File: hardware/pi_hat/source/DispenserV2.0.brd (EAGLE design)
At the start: 65 x 56 mm, 11 parts, among them J10 455-1750-1-ND, J11 455-1750-1-ND, J9 455-1750-1-ND, U2 A4988

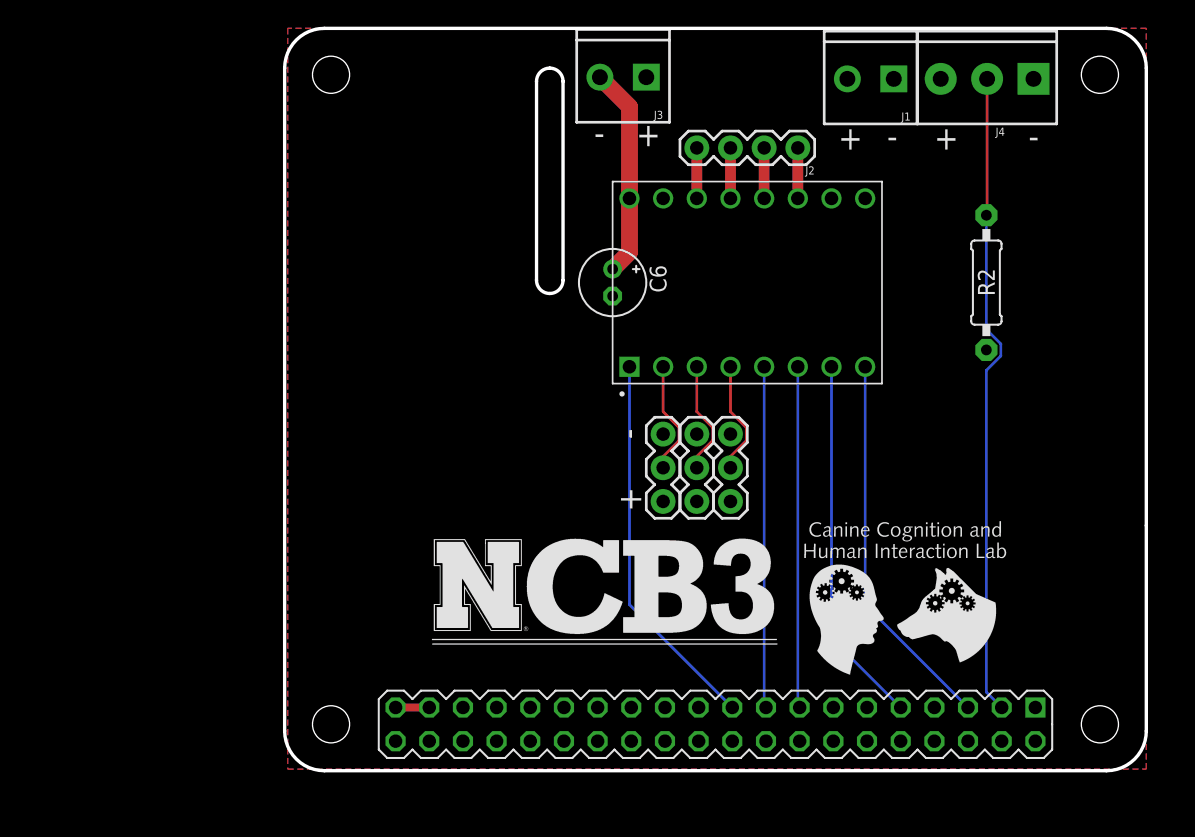
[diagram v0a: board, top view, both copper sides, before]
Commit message: Updated Pi HAT to fix the Pi header pinout
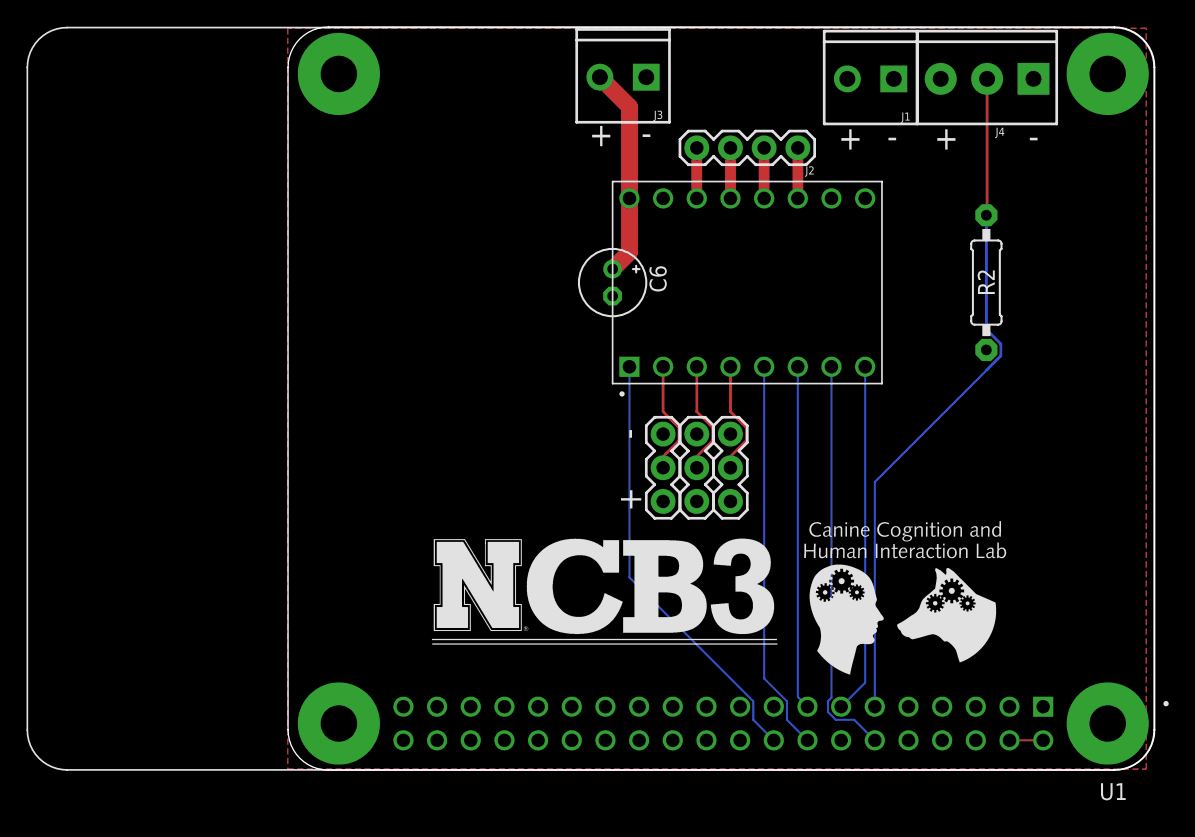
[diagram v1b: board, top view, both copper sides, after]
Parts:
- removed PIE1: PA_RASPI_BPLUS_BRD, PatternAgents-Boards:PA_RASPI_PLATE_BPLUS
- added U1: RASPBERRY_PI_3_MODEL_B+, RASPBERRY_PI_3_MODEL_B_:MODULE_RASPBERRY_PI_3_MODEL_B+
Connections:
- net !ENABLE: now also U1.18; no longer PIE1.19
- net !RESET: now also U1.16; no longer PIE1.17
- net !SLEEP: now also U1.15; no longer PIE1.15
- net 3.3V: now also U1.1, U1.17; no longer PIE1.24, PIE1.40
- net BREAK: now also U1.11; no longer PIE1.3
- net DIR: now also U1.13; no longer PIE1.5
- net GND: now also U1.14, U1.20, U1.25, U1.30, U1.34, U1.39, U1.6, U1.9, U1.S1, U1.S2, U1.S3, U1.S4; no longer PIE1.11, PIE1.16, PIE1.2, PIE1.21, PIE1.27, PIE1.32, PIE1.35, PIE1.7
- net STEP: now also U1.12; no longer PIE1.9
- net V_USB: now also U1.2, U1.4; no longer PIE1.37, PIE1.39
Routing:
- net !ENABLE: track 28.9 -> 32.7 mm
- net !RESET: track 25.8 -> 29.5 mm
- net BREAK: track 48.8 -> 51.8 mm
- net STEP: track 27.9 -> 30.6 mm
- net DIR: track 28.9 -> 26.4 mm
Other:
- board size 65 x 56 mm -> 65.4 x 56.1 mm
